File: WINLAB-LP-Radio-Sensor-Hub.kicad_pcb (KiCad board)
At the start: 2 copper layers, 65 x 55 mm, 80 parts, among them J1 FTSH-105-01-L-DV-K-A, J2 USB_C_Receptacle_USB2.0_16P, J3 Conn_01x02, J4 Conn_Coaxial, J5 Conn_Coaxial, J6 Conn_01x05, J7 Conn_01x05, J8 Conn_01x05, J9 Conn_01x05, Q1 AO3401A, Q2 AO3401A, Q3 AO3401A, U1 EFR32FG23L020F128GM40-C, U2 Si7021-A20, U3 CN3063, U4 TLV74033PDBVR, U5 CH340N, U6 TPS7A0533PDBV, U7 ADG902BRMZ, U8 TPS3839K33DBZ, Y1 39MHz 10pF

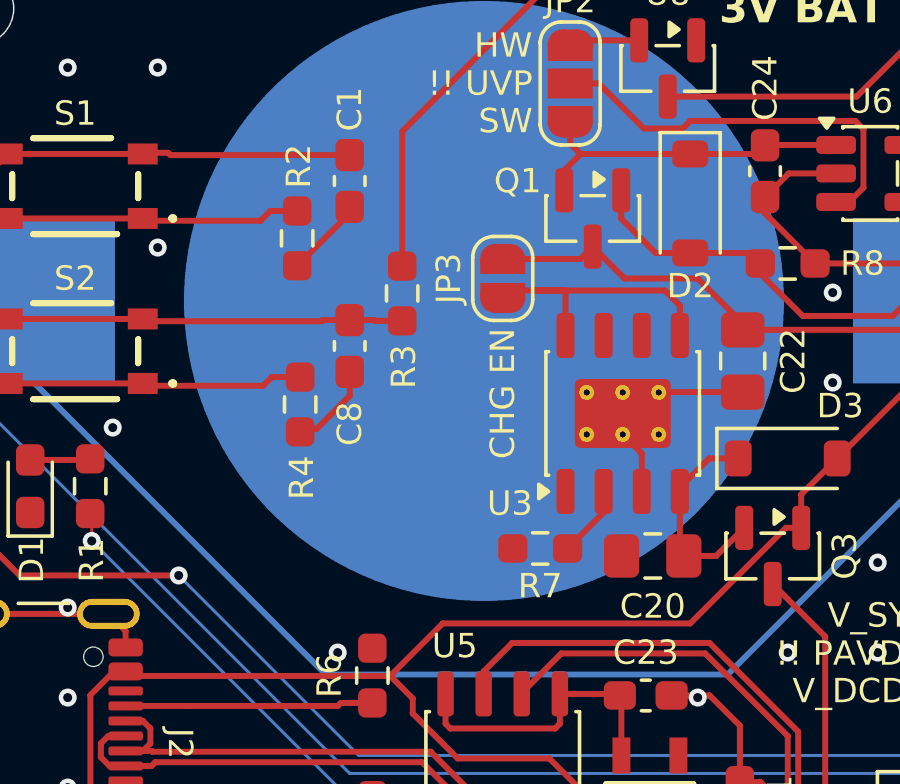
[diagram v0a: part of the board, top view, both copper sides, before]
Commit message: add CHG and DONE LEDs for CN3063
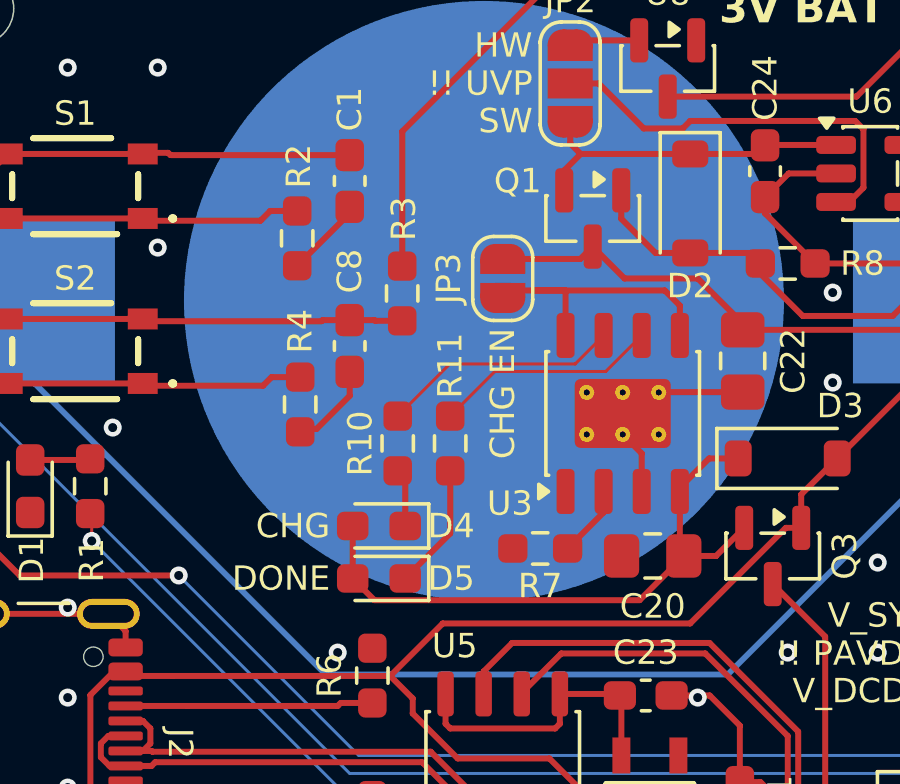
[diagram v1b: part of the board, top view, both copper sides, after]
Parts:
- added D4: LED, LED_SMD:LED_0603_1608Metric_Pad1.05x0.95mm_HandSolder, F.Cu at (199.9, 48.8)
- added D5: LED, LED_SMD:LED_0603_1608Metric_Pad1.05x0.95mm_HandSolder, F.Cu at (199.9, 50.5)
- added R10: 1k, Resistor_SMD:R_0603_1608Metric_Pad0.98x0.95mm_HandSolder, F.Cu at (200.5, 46.0)
- added R11: 1k, Resistor_SMD:R_0603_1608Metric_Pad0.98x0.95mm_HandSolder, F.Cu at (202.2, 46.0)
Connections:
- U3 pad 6: unconnected-(U3-~{DONE}-Pad6) -> Net-(U3-~{DONE})
- U3 pad 7: unconnected-(U3-~{CHRG}-Pad7) -> Net-(U3-~{CHRG})
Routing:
- net Net-(D3-K): track 7.08 -> 20.8 mm
- net Net-(U3-~{CHRG}): track 0.00 -> 7.98 mm
- net Net-(U3-~{DONE}): track 0.00 -> 7.50 mm
- net Net-(D5-K): track 0.00 -> 4.21 mm
- net Net-(D4-K): track 0.00 -> 1.94 mm
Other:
- board text added: "CHG"
- board text added: "DONE"

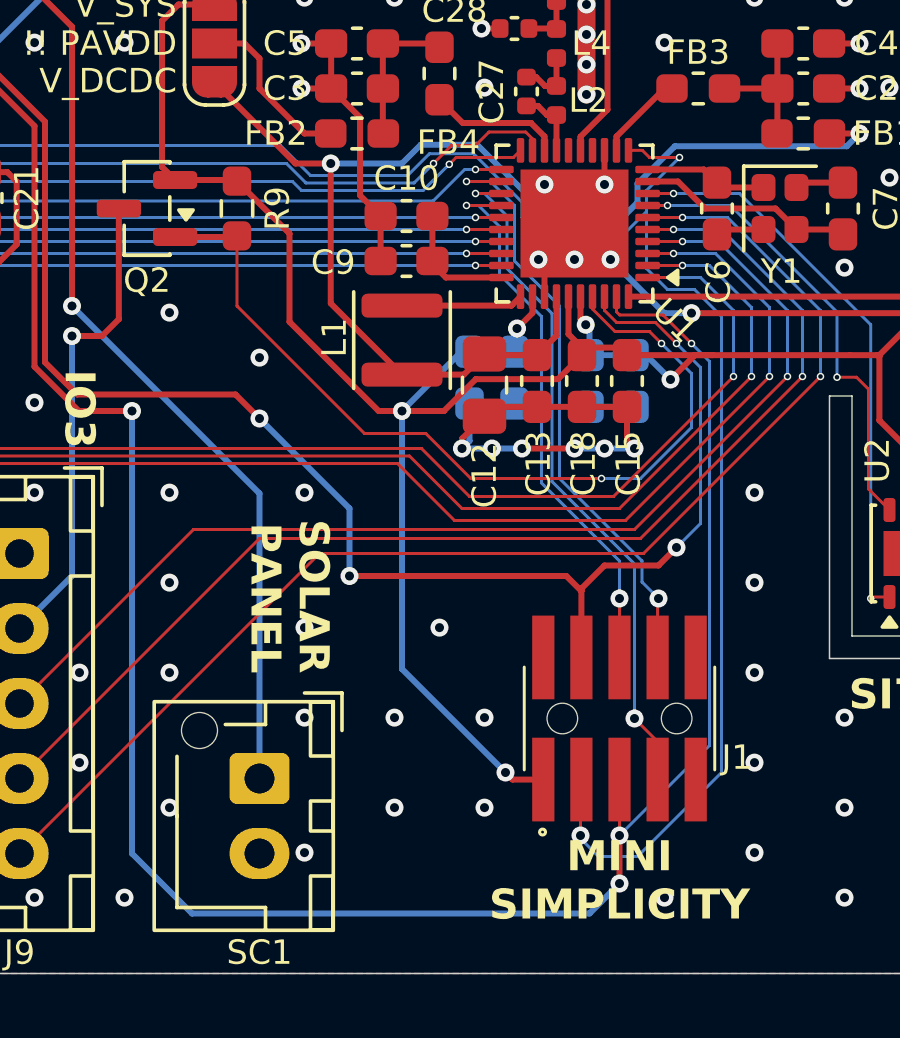
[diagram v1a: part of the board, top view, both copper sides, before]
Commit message: swap VCOM TX and RX lines on SWD connector (redo routing)
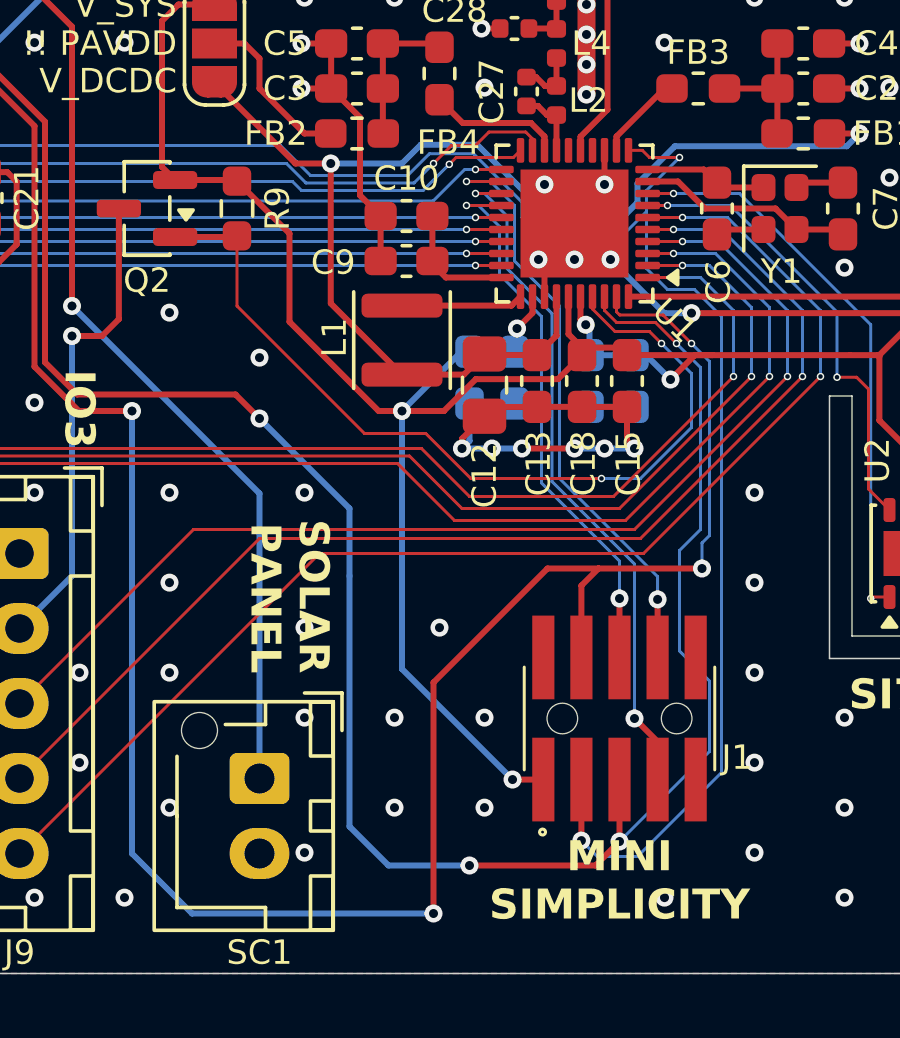
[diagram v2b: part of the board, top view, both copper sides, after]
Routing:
- net VCOM_RX: track 60.0 -> 77.8 mm
- net VCOM_TX: track 79.5 -> 80.8 mm

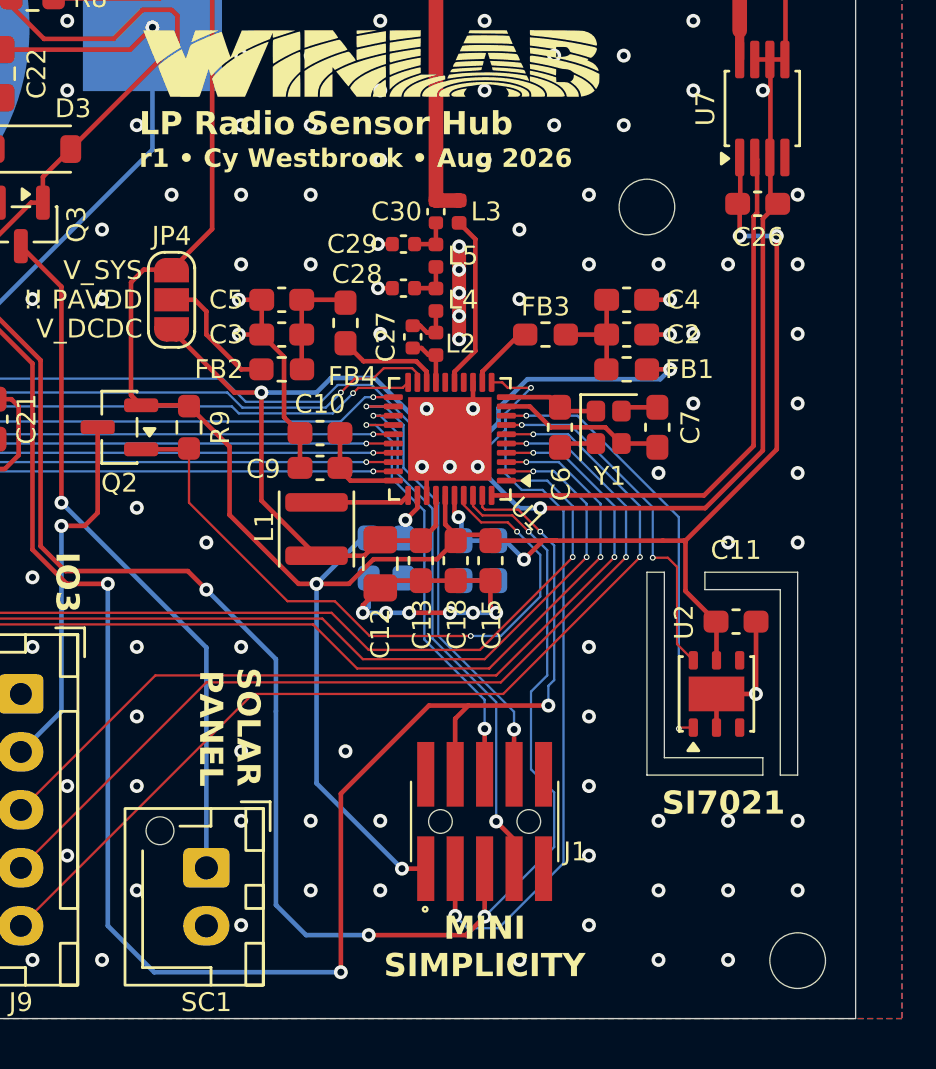
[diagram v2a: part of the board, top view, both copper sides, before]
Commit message: layout and silkscreen tweaks
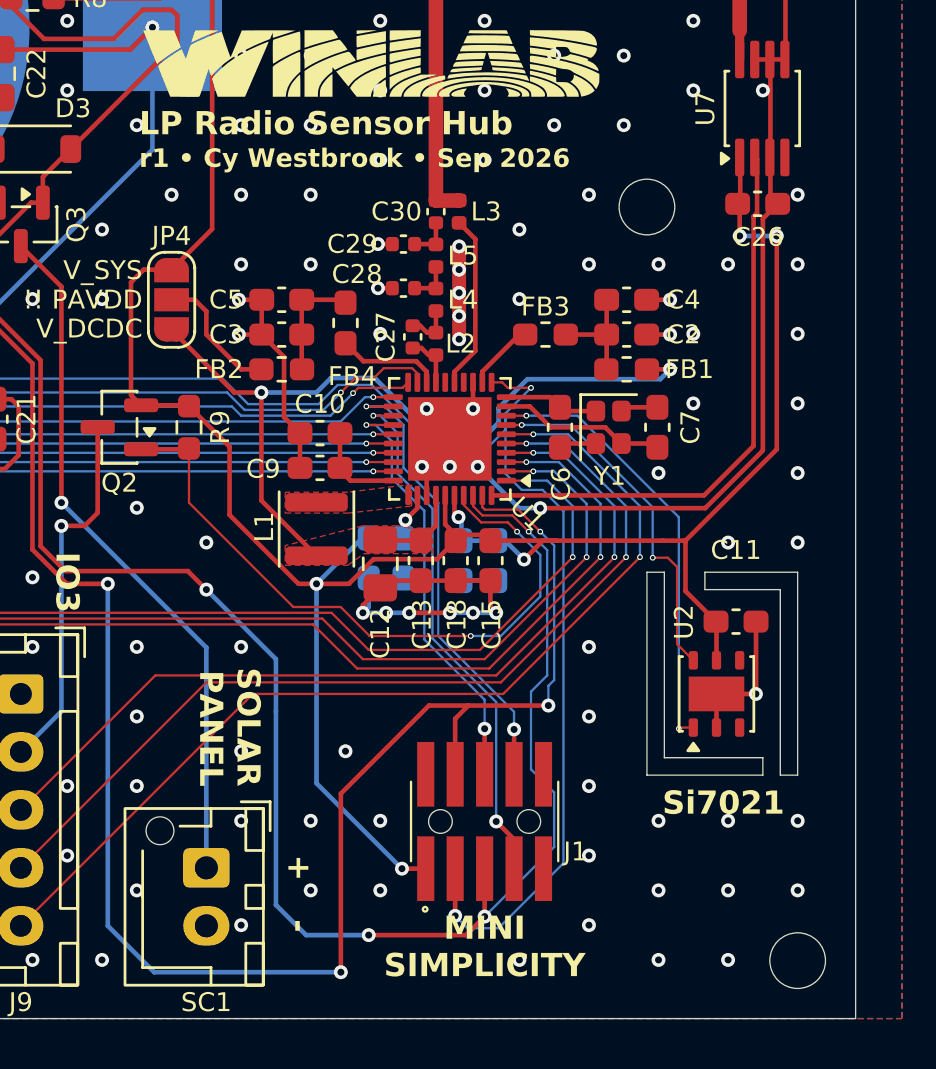
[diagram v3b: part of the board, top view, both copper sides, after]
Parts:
- FB1: value FerriteBead -> BLM18SG700TZ1D
- FB2, FB3: value FerriteBead -> 0R
- FB4: value FerriteBead -> BLM18PG330SN1D
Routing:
- net Net-(U1-VREGSW): track 4.07 -> 0.00 mm
- net EFR32_DCDC: track 41.2 -> 38.9 mm
- added copper zone on F.Cu, net EFR32_DCDC
- added copper zone on F.Cu, net Net-(U1-VREGSW)
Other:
- board text added: "Si7021"
- board text added: "r1 • Cy Westbrook • Sep 2026"
- board text removed: "SI7021"
- board text removed: "r1 • Cy Westbrook • Aug 2026"

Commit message: change CN3063 input diode and tie temp to ground, HW UVP LPF, change DCDC input capacitance setup, remove crystal loading caps, add series resistors on CH340 serial lines, add via fence on CPWGs
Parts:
- removed C6, C7: 12p, Capacitor_SMD:C_0603_1608Metric_Pad1.08x0.95mm_HandSolder
- added C31: 1u, Capacitor_SMD:C_0603_1608Metric_Pad1.08x0.95mm_HandSolder, F.Cu at (212.1, 33.8)
- added R12: 330, Resistor_SMD:R_0603_1608Metric_Pad0.98x0.95mm_HandSolder, F.Cu at (208.8, 52.5)
- added R13: 330, Resistor_SMD:R_0603_1608Metric_Pad0.98x0.95mm_HandSolder, F.Cu at (204.2, 52.5)
- added R14: 10k, Resistor_SMD:R_0603_1608Metric_Pad0.98x0.95mm_HandSolder, F.Cu at (215.8, 34.4)
- C19: value 1u -> 10u
- C25: value 22u -> 4.7u
- D3: value 1N4148W -> B5819W
- R8: value 36k -> 10k
- moved Y1 1.41 mm to (236.9, 58.4)
- moved C24 0.60 mm to (213.3, 37.1)
- moved R6 0.36 mm to (199.3, 53.8)
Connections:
- U3 pad 1: unconnected-(U3-TEMP-Pad1) -> GND
- U5 pad 6: VCOM_TX -> Net-(U5-TXD)
- U5 pad 7: VCOM_RX -> Net-(U5-RXD)
- U8 pad 3: V_BAT -> Net-(U8-VDD)
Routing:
- net GND: track 196.1 -> 187.3 mm, vias 206 -> 246
- net V_BAT: track 82.2 -> 75.4 mm
- net Net-(U8-VDD): track 0.00 -> 5.62 mm
- net VCOM_TX: track 80.8 -> 75.4 mm
- net Net-(U5-TXD): track 0.00 -> 4.00 mm
- net Net-(U1-HFXTAL_I): track 7.24 -> 4.16 mm
- net VCOM_RX: track 77.8 -> 75.4 mm
- net Net-(U5-RXD): track 0.00 -> 2.21 mm
- net +V_SYS: track 144.3 -> 145.9 mm
- net Net-(U1-HFXTAL_O): track 4.11 -> 2.65 mm
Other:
- board text added: "BAT"
- board text removed: "3V BAT"
